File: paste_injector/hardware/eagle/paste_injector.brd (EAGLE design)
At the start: 40 x 30 mm, 16 parts, among them J1 USB, Q1 CSTCR6M00G53Z, U1 ATMEGA328TQFP32, U2 ULN2003AD

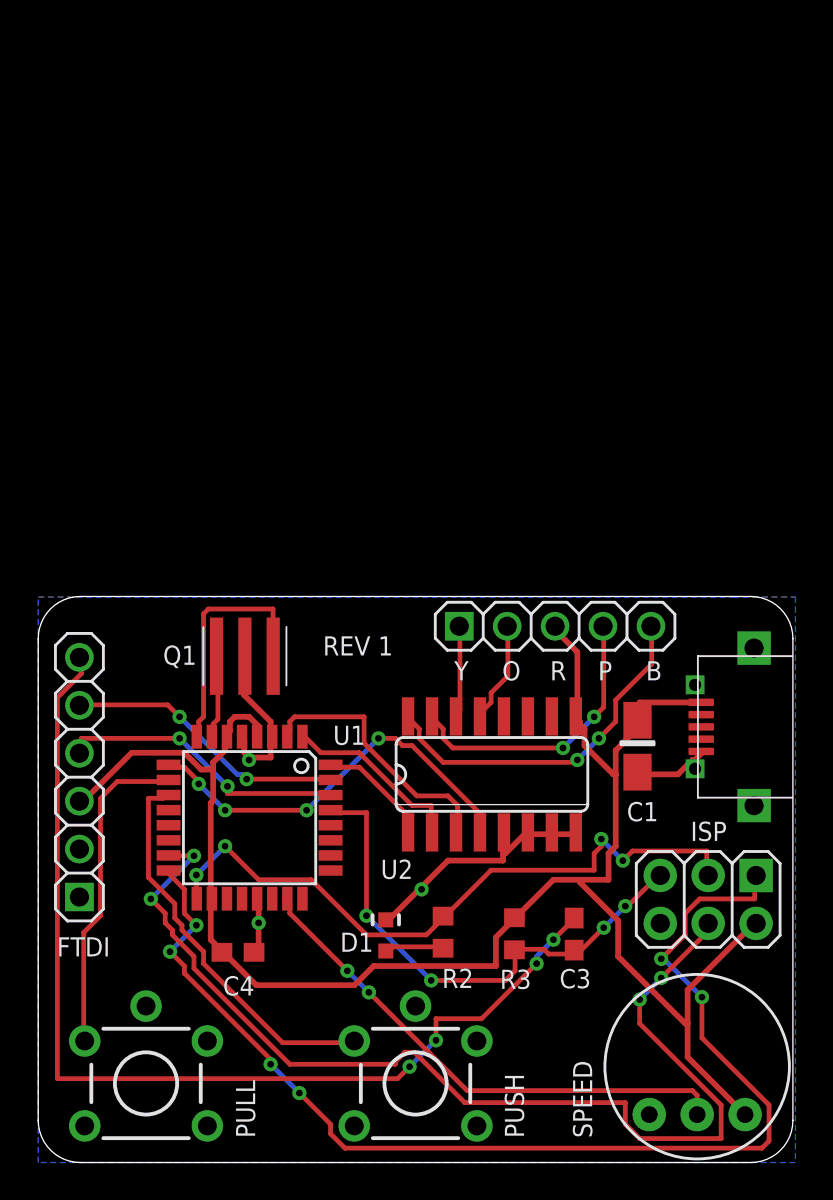
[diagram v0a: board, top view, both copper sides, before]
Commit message: added oled
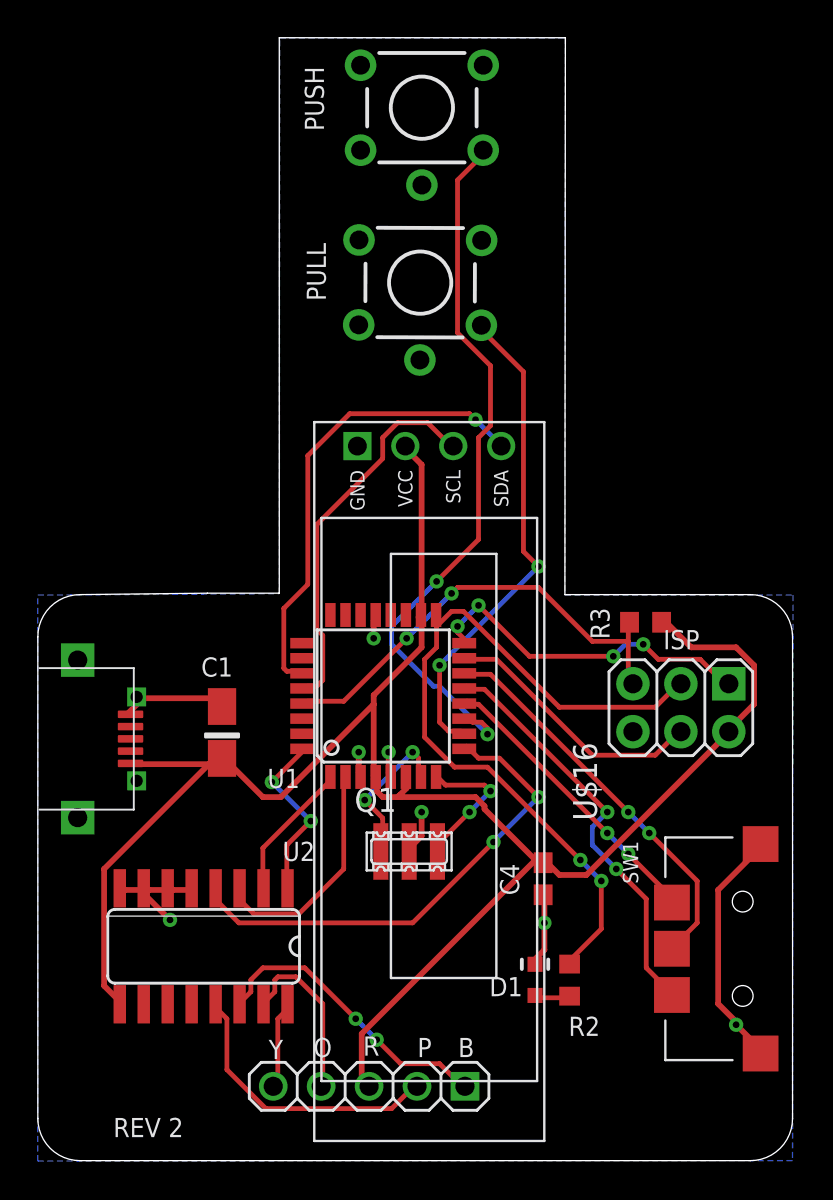
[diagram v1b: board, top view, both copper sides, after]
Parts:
- removed C3: 0.1uF, paste_injector:C0603
- removed J2: (no value), paste_injector:1X06
- removed R1: 10K, paste_injector:TRIMPOT
- added SW1: MCPL3-AV-V, lbrzak:MCPL3-AC-V
- added U$16: DISPLAY-OLED-128X32, diy-modules:DISPLAY-OLED-128X32
- Q1: value CSTCR6M00G53Z -> 16Mhz; device paste_injector:CSTCR6M -> adafruit:CSTCR-G
- moved S2 51.7 mm to (20.3, 55.9), turned to 270 degrees
- moved S1 44.9 mm to (20.2, 46.6), turned to 269.8 degrees
- moved J1 41.1 mm to (-0.53, 22.5), turned to 270 degrees
- moved J3 26.3 mm to (17.5, 4.04), turned to 180 degrees
- moved C1 22.0 mm to (9.74, 22.8), turned to 270 degrees
- moved R3 17.9 mm to (32.2, 28.6), turned to 0 degrees
- moved U2 17.8 mm to (8.77, 11.5), turned to 180 degrees
- moved C4 16.6 mm to (26.8, 15.0), turned to 270 degrees
- moved Q1 13.5 mm to (19.7, 16.5)
- moved ISP 10.3 mm to (34.1, 24.1)
- moved U1 9.58 mm to (18.3, 24.7), turned to 90 degrees
- moved D1 8.25 mm to (26.3, 9.68)
- moved R2 7.17 mm to (28.2, 9.67)
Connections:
- removed net DTR: C3.2, J2.6
- removed net POT: R1.C, U1.23
- new net N$3: U$16.4, U1.27
- new net N$4: U$16.3, U1.28
- new net N$5: SW1.1, U1.12
- new net N$6: SW1.2, U1.13
- new net N$8: SW1.PUSH, U1.14
- net +5V: now also U$16.2; no longer J2.3, R1.CW
- net GND: now also SW1.C, SW1.G, U$16.1; no longer J2.1, J2.2, R1.CCW
- net RESET: no longer C3.1
- net RXI: no longer J2.4
- net TXO: no longer J2.5
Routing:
- net DTR: track 54.8 -> 0.00 mm, vias 4 -> 0
- net MISO: track 62.7 -> 18.4 mm, vias 6 -> 4
- net MOSI: track 57.0 -> 14.2 mm, vias 4 -> 0
- net POT: track 27.6 -> 0.00 mm, vias 2 -> 0
- net N$3: track 0.00 -> 24.8 mm, vias 0 -> 1
- net N$6: track 0.00 -> 22.2 mm, vias 0 -> 2
- net N$8: track 0.00 -> 21.1 mm, vias 0 -> 2
- net N$4: track 0.00 -> 20.3 mm
- net PUSH: track 20.9 -> 38.6 mm, vias 0 -> 2
- net N$5: track 0.00 -> 15.7 mm, vias 0 -> 2
- net RXI: track 15.6 -> 0.00 mm, vias 2 -> 0
- net TXO: track 15.1 -> 0.00 mm, vias 2 -> 0
- net M1-BLUE: track 19.2 -> 4.82 mm, vias 2 -> 0
- net M3-YELOW: track 4.90 -> 15.8 mm, vias 0 -> 2
- net M4-ORANGE: track 5.43 -> 15.2 mm
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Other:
- board size 40 x 30 mm -> 40 x 59.5 mm
- board text added: "REV 2"
- board text removed: "FTDI"
- board text removed: "REV 1"
- board text removed: "SPEED"

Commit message: make board
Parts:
- removed S1, S2: PUSH_BUTTON, paste_injector:PUSH_BUTTON
- removed U$16: DISPLAY-OLED-128X32, diy-modules:DISPLAY-OLED-128X32
- added P-BUTT.: (no value), jumper:JP2
- added U3: DISPLAY-OLED-128X32, diy-modules:DISPLAY-OLED-128X32
- moved R2 16.0 mm to (37.1, 23.0)
- moved D1 14.7 mm to (37.2, 19.6), turned to 180 degrees
- moved R3 11.8 mm to (26.5, 18.2), turned to 270 degrees
- moved J3 9.08 mm to (8.49, 3.23)
- moved Q1 5.84 mm to (19.5, 10.6)
- moved ISP 4.92 mm to (31.3, 20.0), turned to 90 degrees
- moved SW1 2.69 mm to (37.4, 8.64)
- moved U1 2.45 mm to (18.5, 22.3)
- moved C4 2.24 mm to (28.6, 13.8)
- moved U2 2.13 mm to (6.63, 11.4)
- moved C1 1.96 mm to (7.79, 22.7)
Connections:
- net +5V: now also U3.2; no longer U$16.2
- net GND: now also P-BUTT..3, U3.1; no longer S1.A1, S1.GND, S2.A1, S2.GND, U$16.1
- net N$3: now also U3.4; no longer U$16.4
- net N$4: now also U3.3; no longer U$16.3
- net PULL: now also P-BUTT..1; no longer S1.B1
- net PUSH: now also P-BUTT..2; no longer S2.B1
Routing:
- net M4: track 26.1 -> 59.7 mm
- net PUSH: track 38.6 -> 18.3 mm, vias 2 -> 0
- net PULL: track 26.2 -> 10.1 mm
- net SCK/LED: track 40.9 -> 26.1 mm, vias 2 -> 0
- net +5V: track 104.0 -> 92.3 mm
- net GND: track 36.6 -> 27.9 mm
- net M1-BLUE: track 4.82 -> 11.7 mm
- net MOSI: track 14.2 -> 8.99 mm, vias 0 -> 1
- net N$3: track 24.8 -> 19.9 mm, vias 1 -> 2
- net M4-ORANGE: track 15.2 -> 19.9 mm
- net M3-YELOW: track 15.8 -> 11.6 mm, vias 2 -> 0
- net N$6: track 22.2 -> 26.0 mm
- net N$2: track 8.31 -> 12.0 mm
- net M1: track 9.62 -> 6.46 mm, vias 2 -> 0
- net N$8: track 21.1 -> 24.2 mm
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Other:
- board size 40 x 59.5 mm -> 40 x 39.2 mm
- board text removed: "PULL"
- board text removed: "PUSH"
